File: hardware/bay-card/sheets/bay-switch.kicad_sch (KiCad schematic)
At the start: 14 parts, among them Q1 P-FET -30V 6A DFN3x3, Q2 P-FET -30V 6A DFN3x3, Q3 2N7002, Q4 2N7002

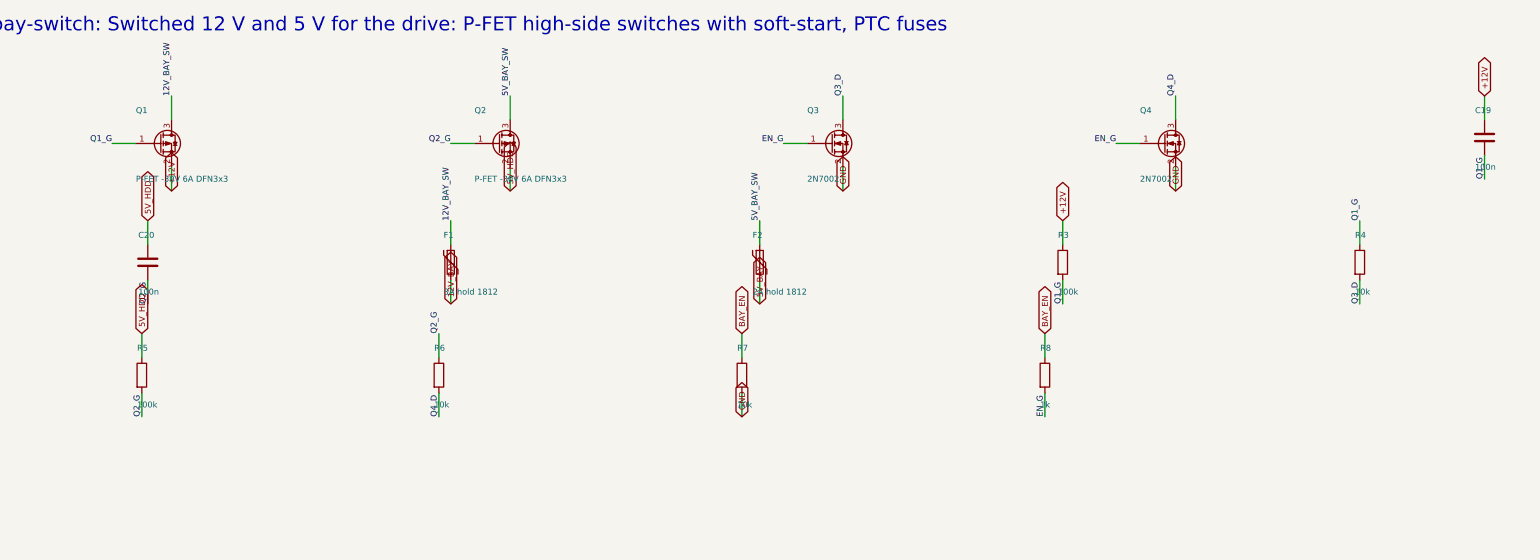
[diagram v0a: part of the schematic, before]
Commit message: hw: 8-pin P-FET symbols (S 1-3, G 4, D 5-8 + EP) for Q20 / Q1 / Q2 — the generic 3-pin symbol had put G/S/D on three source pads; route.py update-nets re-syncs pad nets on a routed board; gen_sch keeps the board design rules; rules restored in both projects
Co-Authored-By: Claude Fable 5.1 <noreply@anthropic.com>
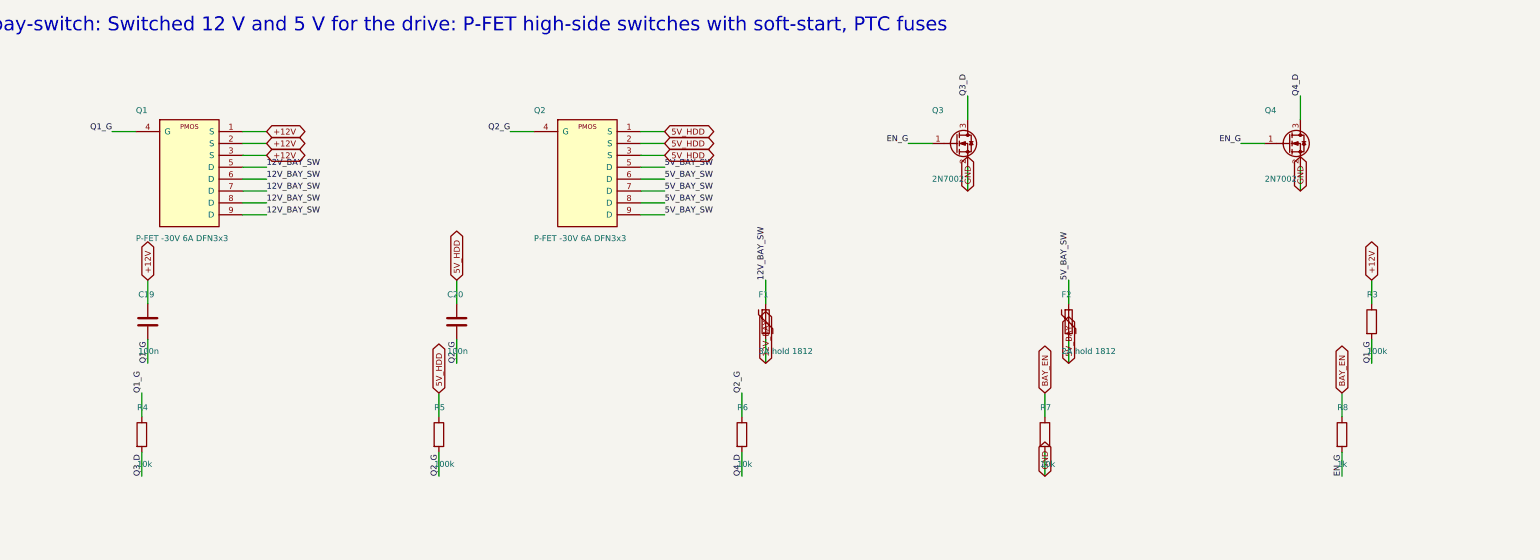
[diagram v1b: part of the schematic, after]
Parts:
- Q1, Q2: symbol Transistor_FET:Q_PMOS_GSD -> brain-drain:PMOS_SSSGDDDD_EP
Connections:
- net +12V: now also Q1.1 (S), Q1.3 (S)
- net 12V_BAY_SW: now also Q1.5 (D), Q1.6 (D), Q1.7 (D), Q1.8 (D), Q1.9 (D); no longer Q1.3 (D)
- net 5V_BAY_SW: now also Q2.5 (D), Q2.6 (D), Q2.7 (D), Q2.8 (D), Q2.9 (D); no longer Q2.3 (D)
- net 5V_HDD: now also Q2.1 (S), Q2.3 (S)
- net Q1_G: now also Q1.4 (G); no longer Q1.1 (G)
- net Q2_G: now also Q2.4 (G); no longer Q2.1 (G)
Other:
- moved on the sheet: C19, C20, F1, F2, Q3, Q4, R3, R4, R5, R6, R7, R8

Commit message: design: bay-card FET is the AOS AON7403 (C25); BOM, STATUS, downloads, decisions
Co-Authored-By: Claude Sonnet 5 <noreply@anthropic.com>
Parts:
- Q1, Q2: value P-FET -30V 6A DFN3x3 -> AON7403
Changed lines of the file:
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@@
 			)
 		)
-		(property "Value" "P-FET -30V 6A DFN3x3"
+		(property "Value" "AON7403"
 			(at 60.96 55.84 0)
 			(effects
@@
 			)
 		)
-		(property "Description" "12 V switch; DFN 3x3-8 power pin-out S 1-3, G 4, D 5-8 + EP"
+		(property "Description" "12 V switch (AOS AON7403, -30 V, DFN 3x3-8); DFN 3x3-8 power pin-out S 1-3, G 4, D 5-8 + EP"
 			(at 72.39 41.91 0)
 			(effects
@@
 			)
 		)
-		(property "Value" "P-FET -30V 6A DFN3x3"
+		(property "Value" "AON7403"
 			(at 146.05 55.84 0)
 			(effects
@@
 			)
 		)
-		(property "Description" "5 V switch; same pin-out"
+		(property "Description" "5 V switch (AOS AON7403); same pin-out"
 			(at 157.48 41.91 0)
 			(effects
